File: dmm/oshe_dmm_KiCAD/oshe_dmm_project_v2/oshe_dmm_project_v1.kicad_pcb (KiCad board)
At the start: 4 copper layers, 88.9 x 165.1 mm, 79 parts, among them J1 FTDI Basic, J10 Voltage Range 2, J11 Voltage Range 3, J12 Voltage Range 3, J13 Current Indication, J2 Voltage, J3 GND, J4 Current, J6 ON/OFF, J7 Voltage Range 1, J8 Voltage Range 1, J9 Voltage Range 2, SW1 PTS526 SK15 SMTR2 LFS, U1 ATmega328P-A, U2 INA219BxD, U3 ADS1115IDGS, U4 MAX4617CPE, U5 LM317_SOT-223, Y1 16MHz

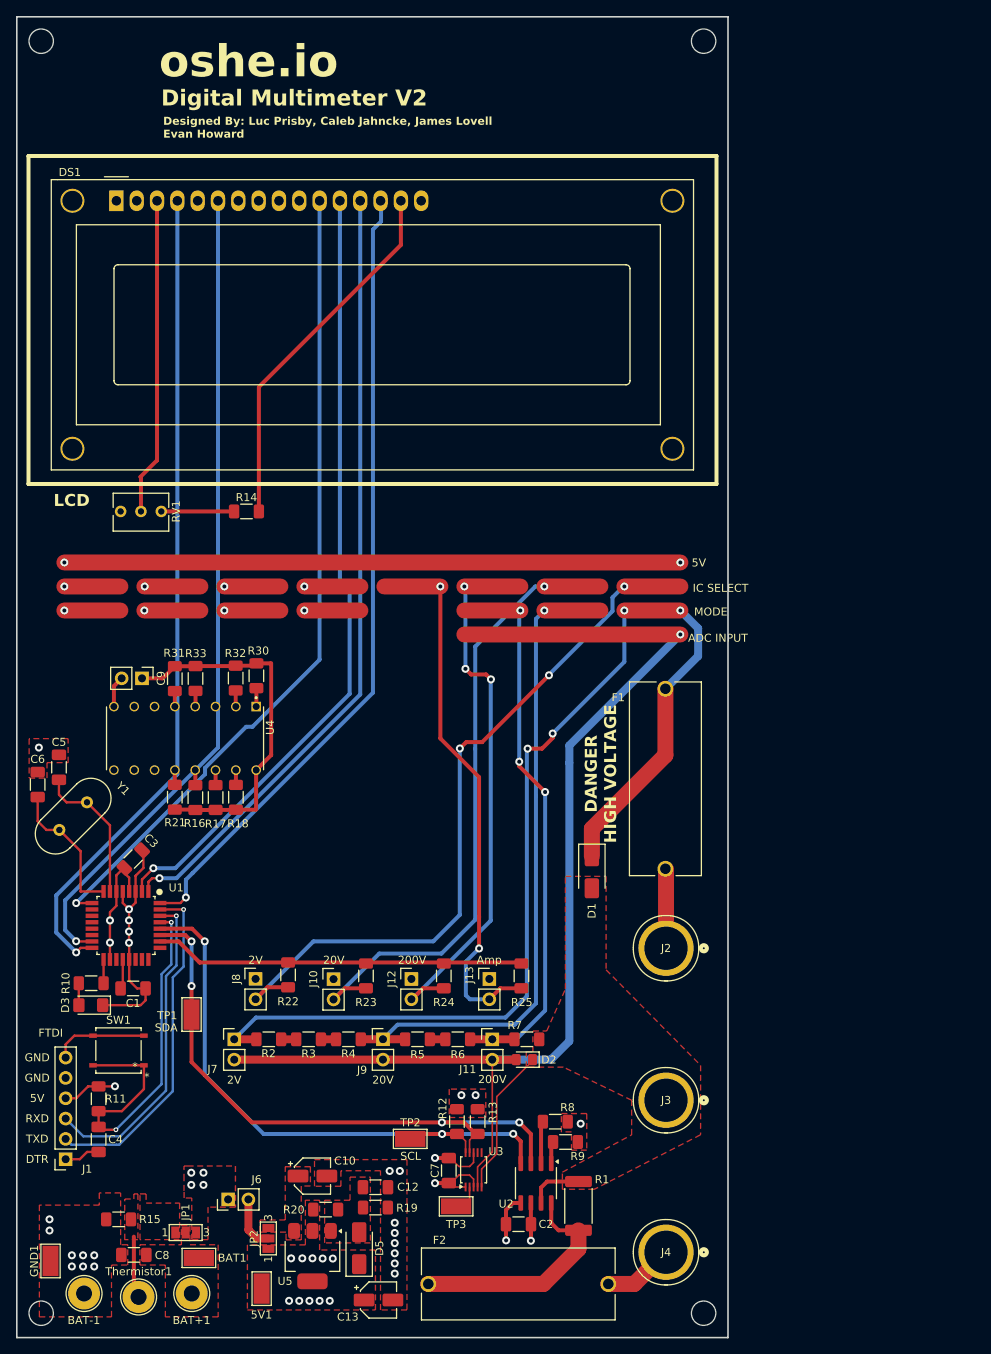
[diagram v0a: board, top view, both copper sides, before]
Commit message: Resistance meas on PCB, need to add lead connections
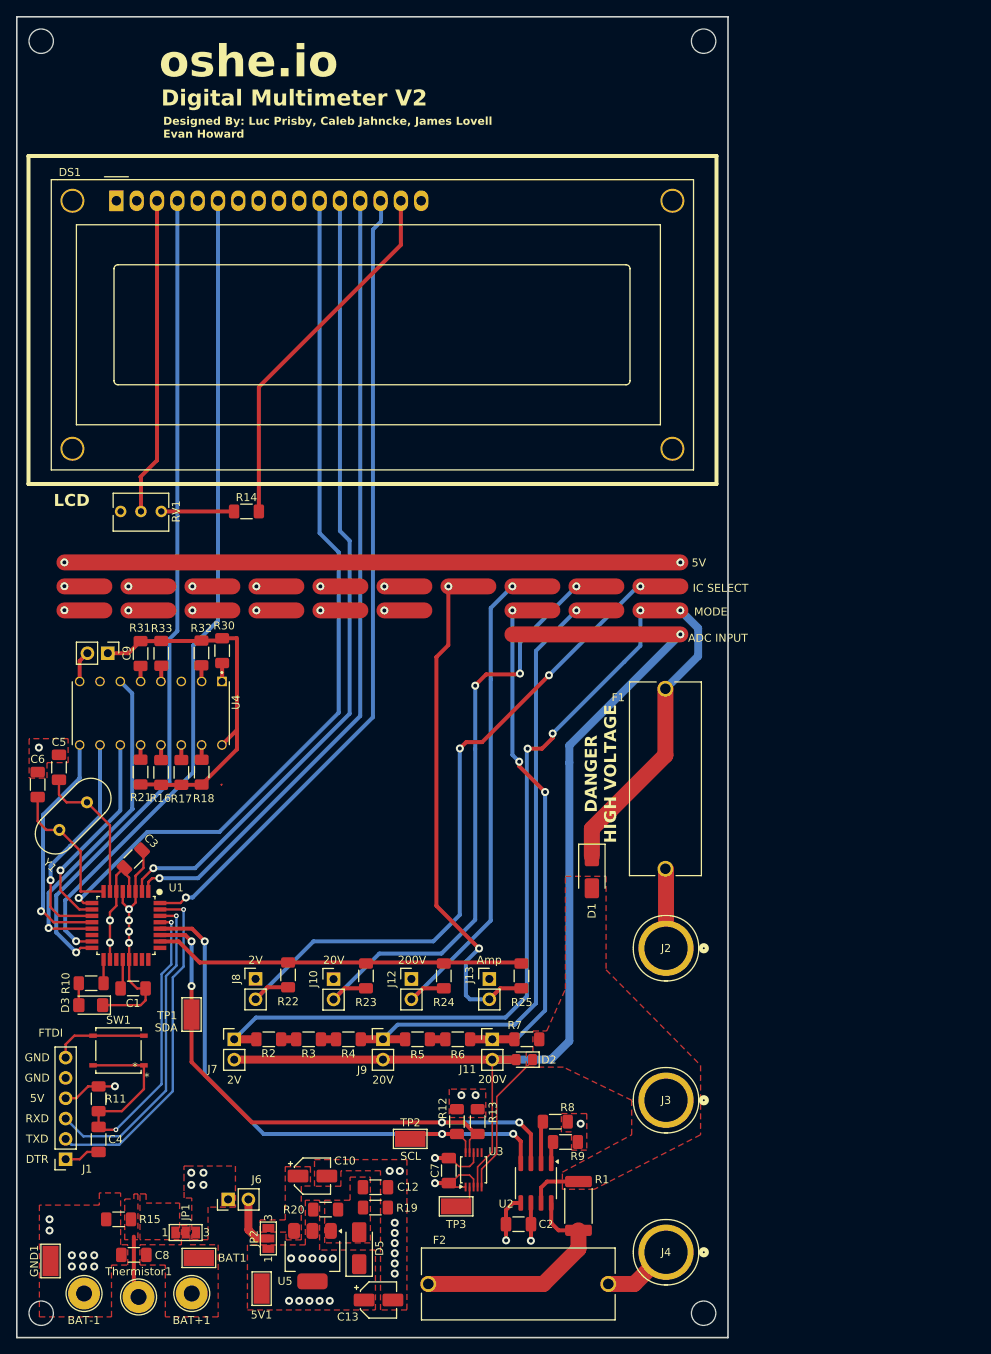
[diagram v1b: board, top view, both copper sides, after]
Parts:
- moved R21 5.31 mm to (135.5, 157.6)
- moved R30 5.31 mm to (145.7, 142.4)
- moved R33 5.31 mm to (138.1, 142.7)
- moved C9 5.31 mm to (131.4, 142.7)
- moved R16 5.31 mm to (138.1, 157.6)
- moved R18 5.31 mm to (143.2, 157.6)
- moved R31 5.31 mm to (135.5, 142.8)
- moved R32 5.31 mm to (143.1, 142.7)
- moved U4 5.31 mm to (136.8, 150.2)
- moved R17 5.31 mm to (140.6, 157.6)
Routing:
- net D9: track 0.00 -> 41.3 mm, vias 0 -> 1
- net D8: track 0.00 -> 29.7 mm, vias 0 -> 1
- net D7: track 0.00 -> 28.5 mm, vias 0 -> 1
- net D6: track 0.00 -> 26.2 mm, vias 0 -> 1
- net D5: track 102.8 -> 109.0 mm
- net Net-(J10-Pin_2): track 72.4 -> 75.8 mm, vias 1 -> 3
- net 20V_Rang: track 76.1 -> 77.7 mm
- net D3: track 99.1 -> 100.7 mm
- net D4: track 99.2 -> 100.6 mm
- net Net-(J12-Pin_2): track 62.9 -> 61.5 mm, vias 3 -> 1
- net +5V: track 90.0 -> 91.3 mm
- net Net-(J8-Pin_2): track 85.4 -> 86.4 mm
- net 2V_Rang: track 133.1 -> 133.9 mm
- net Net-(J13-Pin_2): track 61.5 -> 62.3 mm
- net MOSI/D11: vias 3 -> 1
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
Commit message: finished Resistance
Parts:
- added D4: SMAJ200A, Diode_SMD:D_SMA, F.Cu at (191.2, 147.1)
- added J5: Resistance Meas, Connector_PinHeader_2.54mm:PinHeader_1x02_P2.54mm_Vertical, F.Cu at (232.3, 147.7)
- added R34: R?, Resistor_SMD:R_1206_3216Metric_Pad1.30x1.75mm_HandSolder, F.Cu at (237.6, 151.6)
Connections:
- U4 pad 3: Resistance_Input -> A0
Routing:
- net GND: track 86.4 -> 207.6 mm, vias 24 -> 27
- net A0: track 0.00 -> 109.2 mm, vias 0 -> 5
- net +5V: track 91.3 -> 102.5 mm
- net 2V_Rang: track 133.9 -> 141.9 mm
- net Net-(J8-Pin_2): track 86.4 -> 89.5 mm, vias 3 -> 5
- net Net-(J13-Pin_2): track 62.3 -> 61.2 mm, vias 2 -> 3

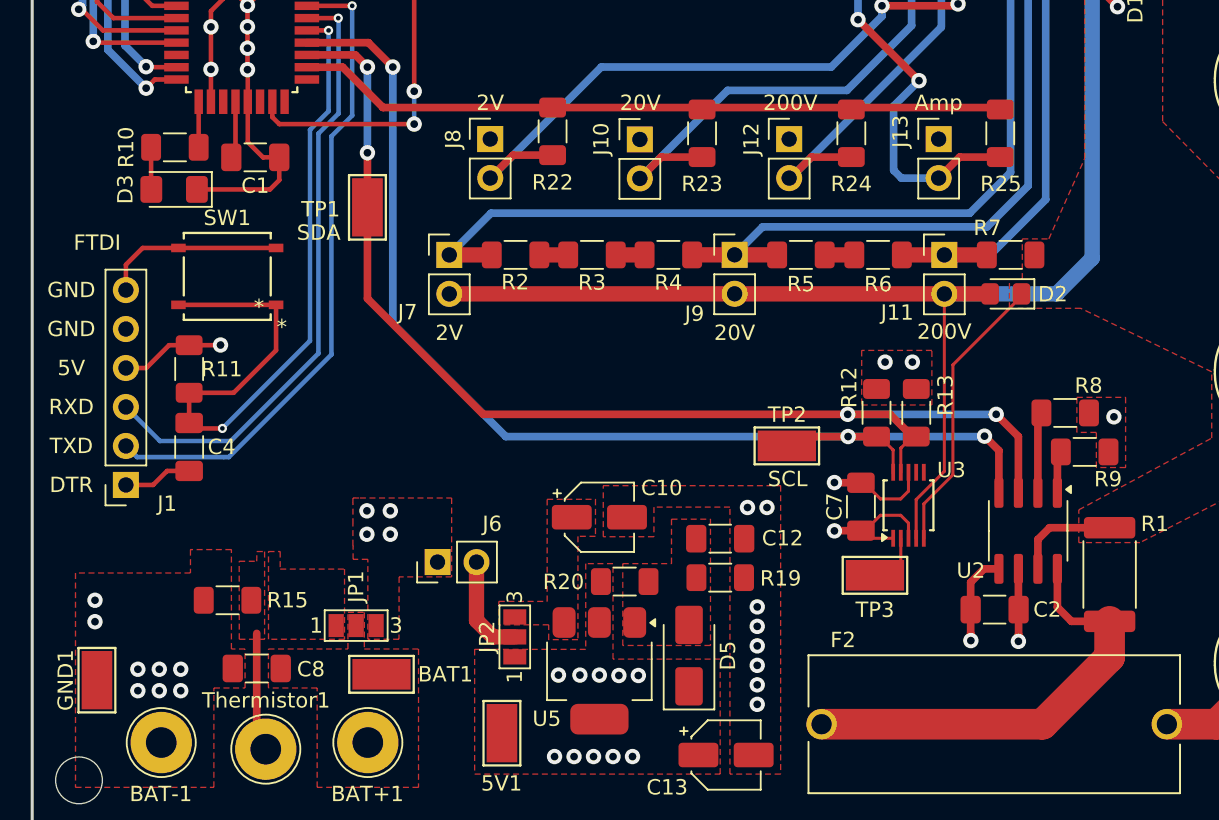
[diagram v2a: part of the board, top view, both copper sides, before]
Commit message: DC Voltage and Current Update
The PCB was updated so that only one ADC is used for DC voltage and current measurement. The footprint for the ADC was also updated.
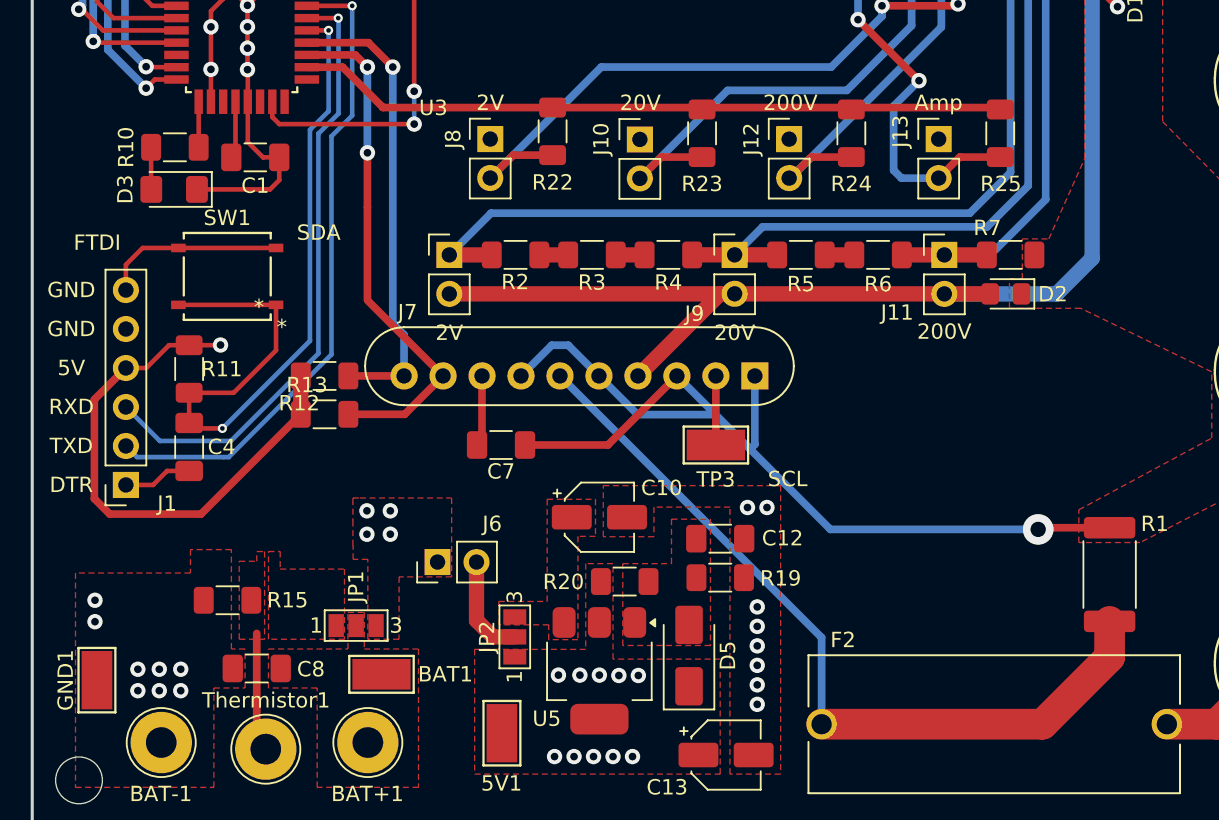
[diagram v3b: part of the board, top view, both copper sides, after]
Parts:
- removed C2: 0.1uF, Capacitor_SMD:C_1206_3216Metric_Pad1.33x1.80mm_HandSolder
- removed R8, R9: 1k, Resistor_SMD:R_1206_3216Metric_Pad1.30x1.75mm_HandSolder
- removed TP1, TP2: SDA, TestPoint:TestPoint_Keystone_5019_Minature
- removed U2: INA219BxD, Package_SO:SOIC-8_3.9x4.9mm_P1.27mm
- U3: footprint Package_SO:TSSOP-10_3x3mm_P0.5mm -> ZC261500:MODULE_ZC261500
- moved R13 38.6 mm to (139.1, 201.4), turned to 0 degrees
- moved R12 36.0 mm to (139.1, 198.9), turned to 0 degrees
- moved U3 26.2 mm to (155.7, 192.2), turned to 0 degrees
- moved C7 23.8 mm to (150.6, 203.4), turned to 180 degrees
- moved TP3 13.4 mm to (164.6, 203.4)
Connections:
- F2 pad 2: Net-(U2-IN+) -> Net-(U3-AIN2)
- R1 pad 1: Net-(U2-IN+) -> Net-(U3-AIN2)
- U3 pad 6: unconnected-(U3-AIN2-Pad6) -> Net-(U3-AIN2)
- U3 pad 7: unconnected-(U3-AIN3-Pad7) -> GND
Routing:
- net Net-(U3-AIN2): track 0.00 -> 52.7 mm
- net SCL: track 77.7 -> 30.3 mm, vias 3 -> 1
- net SDA: track 76.9 -> 33.7 mm, vias 4 -> 2
- net Net-(U2-IN+): track 29.2 -> 0.00 mm
- net GND: track 207.6 -> 232.5 mm, vias 27 -> 25
- net +5V: track 102.5 -> 122.7 mm, vias 19 -> 15
- net V_ADC_Input: track 119.1 -> 110.9 mm
- net Net-(U2-A0): track 4.98 -> 0.00 mm
- net Net-(U2-A1): track 2.70 -> 0.00 mm
